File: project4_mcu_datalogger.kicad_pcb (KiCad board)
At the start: 2 copper layers, 29 parts, among them J1 Conn_01x04_Pin, J2 Conn_01x09_Pin, J3 Conn_01x04_Pin, J4 Conn_02x03_Odd_Even, U1 24LC1025, U2 24LC1025, U3 ATMEGA328P-AU, U4 DS1337S_T_R, Y1 32.768 KHz, Y2 16 MHz

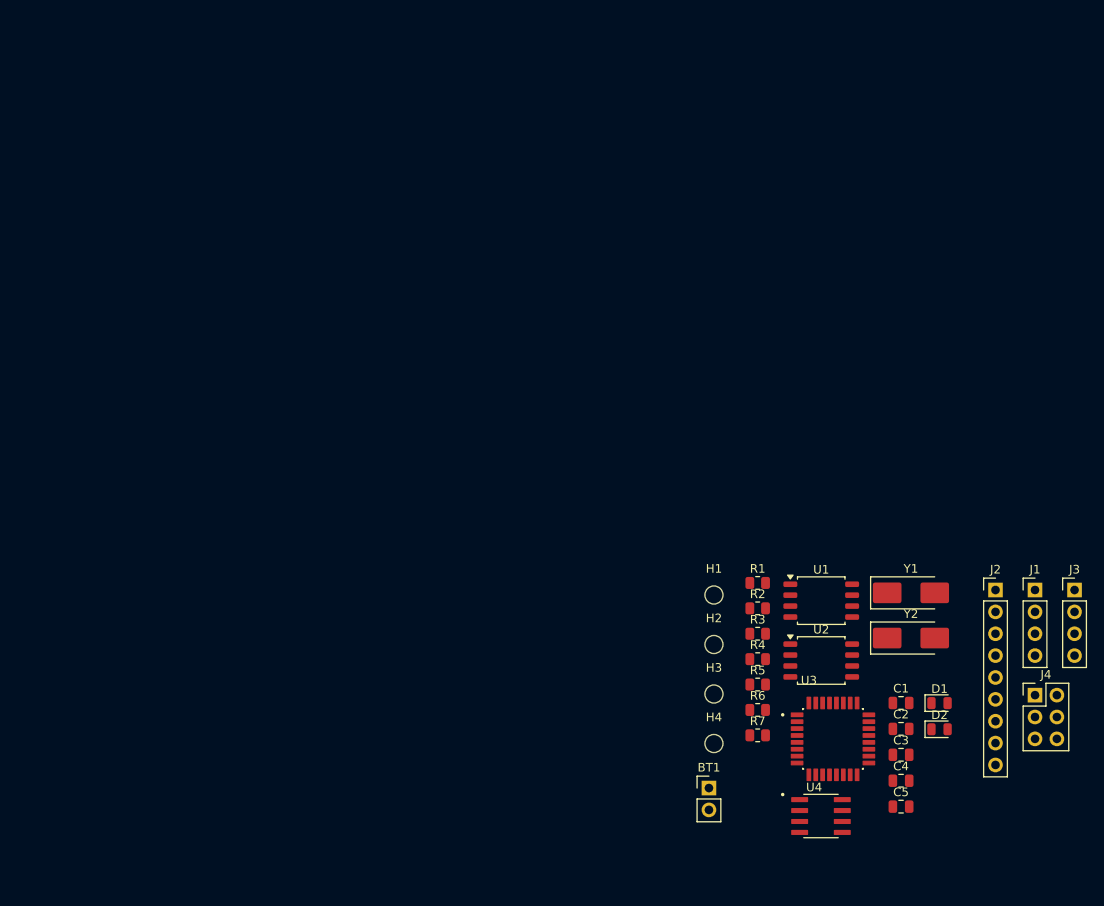
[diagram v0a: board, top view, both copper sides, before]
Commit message: Completed placement of footprints
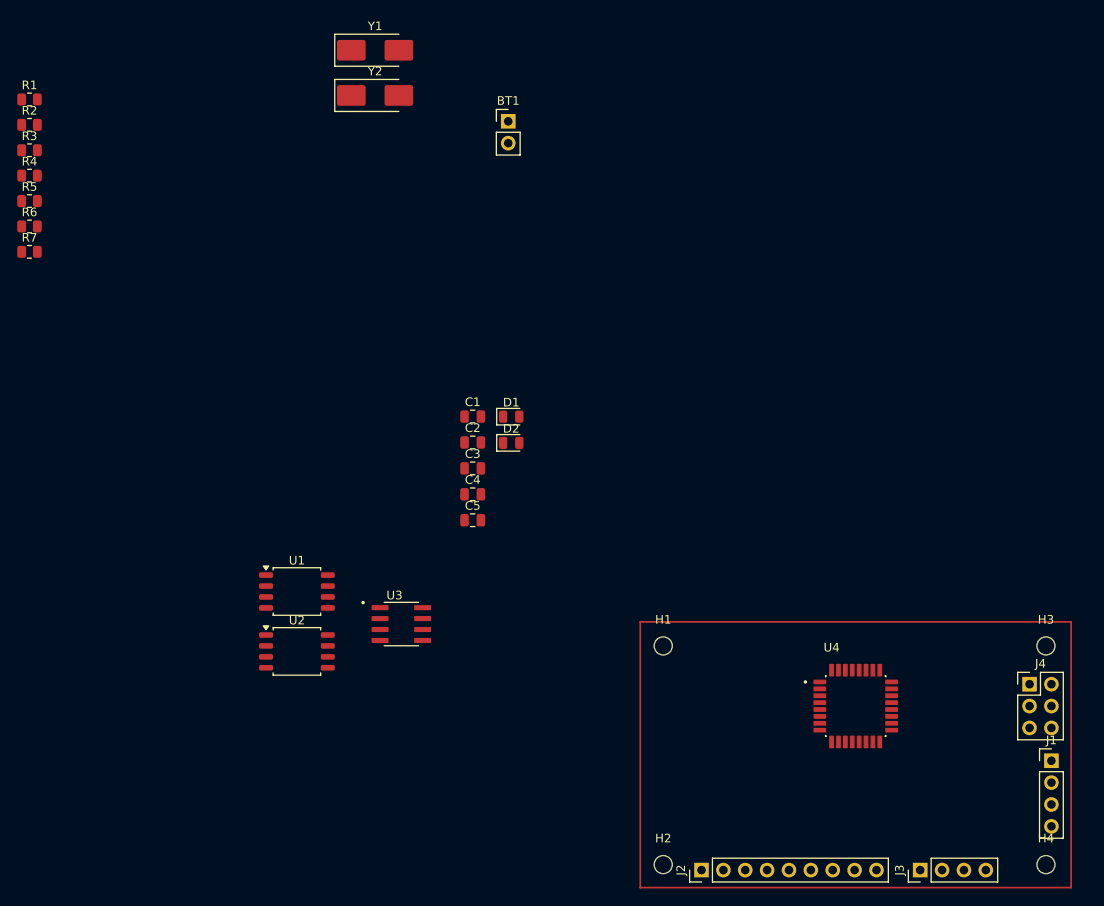
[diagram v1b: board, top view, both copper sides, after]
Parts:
- moved R1 101.5 mm to (54.0, 39.4)
- moved R2 101.5 mm to (54.0, 42.4)
- moved R3 101.5 mm to (54.0, 45.3)
- moved R4 101.5 mm to (54.0, 48.2)
- moved R5 101.5 mm to (54.0, 51.2)
- moved R6 101.5 mm to (54.0, 54.1)
- moved R7 101.5 mm to (54.0, 57.1)
- moved Y1 88.6 mm to (94.2, 33.7)
- moved Y2 88.6 mm to (94.2, 38.9)
- moved BT1 80.9 mm to (109.6, 41.9)
- moved U1 60.9 mm to (85.1, 96.5)
- moved U2 60.9 mm to (85.1, 103.5)
- moved C1 59.8 mm to (105.5, 76.2)
- moved C2 59.8 mm to (105.5, 79.2)
- moved C3 59.8 mm to (105.5, 82.2)
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- renumbered U4 to U3, U3 to U4

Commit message: Completed PCB routing
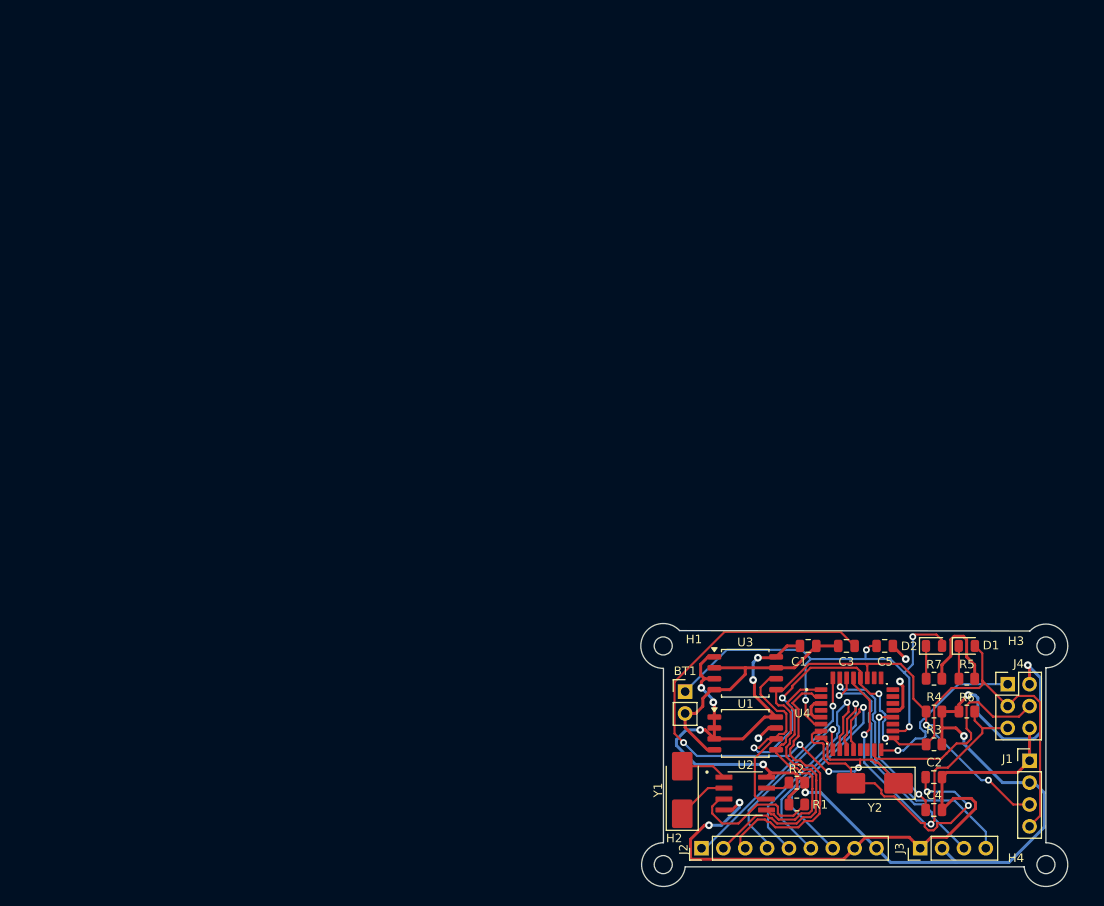
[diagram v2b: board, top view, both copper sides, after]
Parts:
- U2: value 24LC1025 -> DS1337S_T_R; footprint Package_SO:SOIC-8_5.3x5.3mm_P1.27mm -> DS1337S_T_R:SOIC127P600X175-8N
- U3: value DS1337S_T_R -> 24LC1025; footprint DS1337S_T_R:SOIC127P600X175-8N -> Package_SO:SOIC-8_5.3x5.3mm_P1.27mm
- moved R3 125.7 mm to (159.1, 114.3), turned to 180 degrees
- moved R6 122.6 mm to (162.9, 110.5)
- moved R5 122.2 mm to (162.9, 106.7), turned to 180 degrees
- moved R4 122.1 mm to (159.1, 110.5), turned to 180 degrees
- moved R1 121.0 mm to (143.2, 121.3)
- moved R2 117.4 mm to (143.2, 118.7), turned to 180 degrees
- moved R7 116.2 mm to (159.1, 106.7)
- moved Y2 98.7 mm to (152.2, 118.8), turned to 180 degrees
- moved Y1 93.0 mm to (129.8, 119.6), turned to 90 degrees
- moved BT1 69.3 mm to (130.2, 108.2)
- moved C2 66.2 mm to (159.1, 118.1), turned to 180 degrees
- moved C4 64.9 mm to (159.1, 121.9), turned to 180 degrees
- moved D1 59.2 mm to (162.9, 102.9)
- moved U2 54.6 mm to (137.2, 120.0)
- moved U1 54.6 mm to (137.2, 113.0)
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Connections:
- C2 pad 2: Net-(U4-PB7) -> Net-(U4-PB6)
- C3 pad 2: Net-(U4-PB6) -> Net-(U4-PB7)
- R1 pad 2: Net-(U3-~{INTA}) -> Net-(U2-~{INTA})
- R2 pad 2: Net-(U3-SQW/~INT) -> Net-(U2-SQW/~INT)
- U2 pad 1: /Vcc -> Net-(U2-X1)
- U2 pad 2: GND -> Net-(U2-X2)
- U2 pad 3: /Vcc -> Net-(U2-~{INTA})
- U2 pad 7: GND -> Net-(U2-SQW/~INT)
- U3 pad 1: Net-(U3-X1) -> /Vcc
- U3 pad 2: Net-(U3-X2) -> GND
- U3 pad 3: Net-(U3-~{INTA}) -> /Vcc
- U3 pad 7: Net-(U3-SQW/~INT) -> GND
- Y1 pad 1: Net-(U3-X2) -> Net-(U2-X2)
- Y1 pad 2: Net-(U3-X1) -> Net-(U2-X1)
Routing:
- net /Vcc: track 0.00 -> 149.1 mm, vias 0 -> 10
- net GND: track 0.00 -> 130.3 mm, vias 0 -> 5
- net /SCK: track 0.00 -> 98.7 mm, vias 0 -> 4
- net Net-(U4-PB7): track 0.00 -> 67.6 mm, vias 0 -> 4
- net /SDA: track 0.00 -> 67.2 mm, vias 0 -> 2
- net Net-(BT1-+): track 0.00 -> 57.7 mm, vias 0 -> 4
- net /RESET: track 0.00 -> 41.2 mm, vias 0 -> 2
- net Net-(U4-PB6): track 0.00 -> 36.0 mm, vias 0 -> 2
- net /D3: track 0.00 -> 33.5 mm
- net /D4: track 0.00 -> 32.9 mm
- net /TX: track 0.00 -> 31.2 mm, vias 0 -> 1
- net /RX: track 0.00 -> 29.2 mm, vias 0 -> 1
- net /D6: track 0.00 -> 27.9 mm, vias 0 -> 1
- net /D7: track 0.00 -> 27.7 mm, vias 0 -> 1
- net /D8: track 0.00 -> 27.5 mm, vias 0 -> 1
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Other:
- board outline added: 49.6 x 30.5 mm

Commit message: Rework of PCB routing
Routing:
- net GND: track 130.3 -> 176.2 mm, vias 5 -> 9
- net Net-(BT1-+): track 57.7 -> 62.2 mm
- net /SDA: track 67.2 -> 66.6 mm

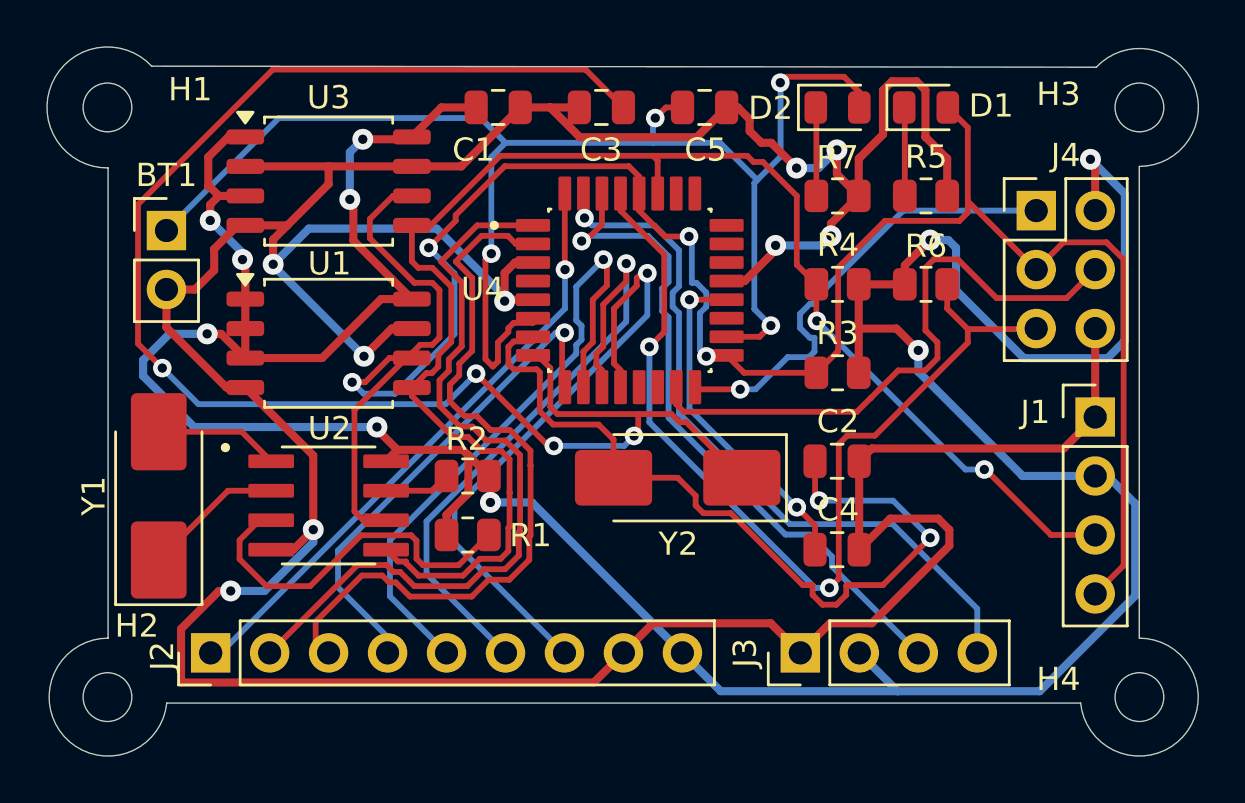
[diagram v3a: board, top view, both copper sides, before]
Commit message: Added copper fills and improved routing
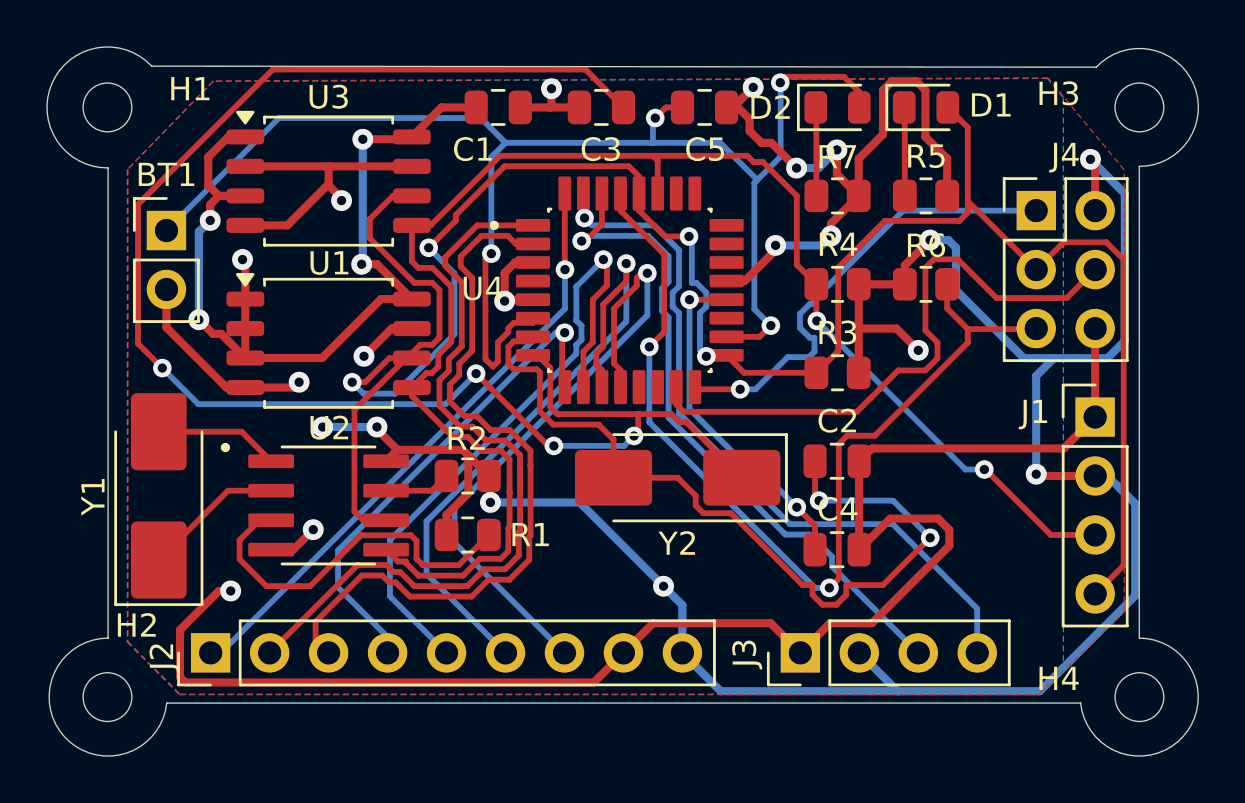
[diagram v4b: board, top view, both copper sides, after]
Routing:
- net GND: track 176.2 -> 131.0 mm, vias 9 -> 12
- net /Vcc: track 149.1 -> 138.3 mm, vias 10 -> 13
- added copper zone on F.Cu, net /Vcc
- added copper zone on B.Cu, net GND

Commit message: Fixed outstanding issues
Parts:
- renumbered J2 to J1, J1 to J2
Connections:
- BT1 pad 1: Net-(BT1-+) -> /Vcc
- C5 pad 1: Net-(BT1-+) -> /Vcc
- D2 pad 2: Net-(BT1-+) -> /Vcc
- U4 pad 18: Net-(BT1-+) -> /Vcc
- U4 pad 6: Net-(BT1-+) -> /Vcc
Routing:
- net Net-(BT1-+): track 62.2 -> 0.00 mm, vias 4 -> 0
- net /Vcc: track 138.3 -> 173.1 mm, vias 13 -> 16
- net GND: track 131.0 -> 138.7 mm, vias 12 -> 11
- net Net-(U2-~{INTA}): track 16.2 -> 20.2 mm
- net Net-(U4-PB7): track 67.6 -> 68.9 mm
- net /SDA: track 66.6 -> 67.9 mm
- net /SCK: track 98.7 -> 99.3 mm
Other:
- board text added: "2"
- board text added: "3"
- board text added: "4"
- board text added: "5"
- board text added: "6"
- board text added: "7"
- board text added: "8"
- board text added: "GND"
- board text added: "GPIO"
- board text added: "I2C"
- board text added: "ICSP"
- board text added: "ICSP MISO | Vcc SCK | MOSI RESET | GND"
- board text added: "RX"
- board text added: "SCK"
- board text added: "SDA"
- board text added: "SERIAL"
- board text added: "TX"
- board text added: "Vcc"

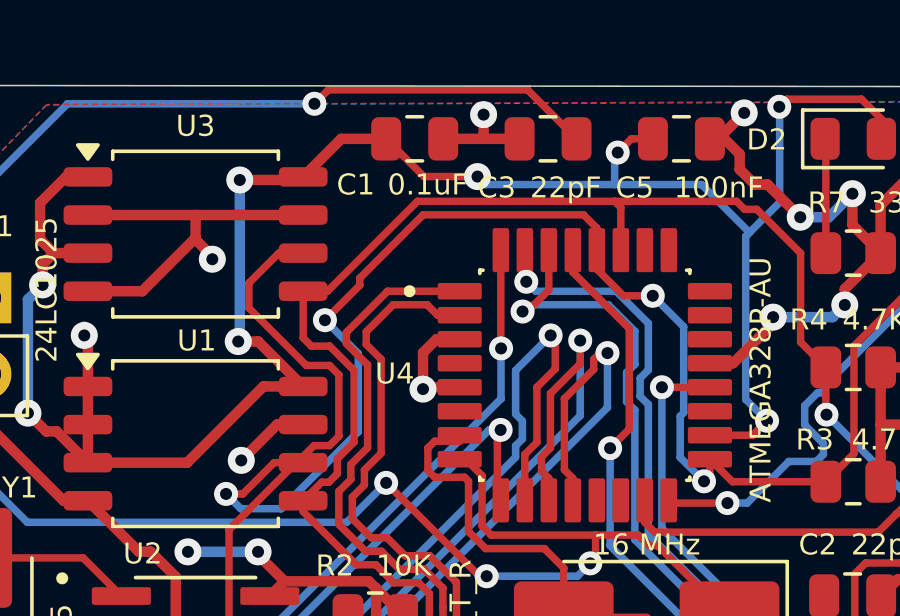
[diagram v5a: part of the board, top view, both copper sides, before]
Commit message: Added back silkscreen
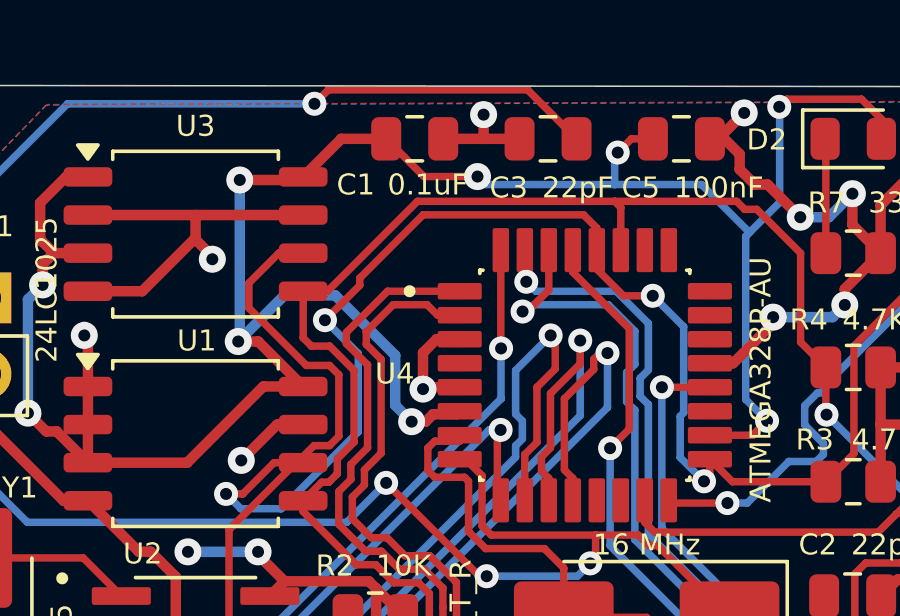
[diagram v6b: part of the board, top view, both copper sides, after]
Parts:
- added REF**: KiCad-Logo2_5mm_SilkScreen, Symbol:KiCad-Logo2_5mm_SilkScreen, B.Cu at (139.1, 106.0)
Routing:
- net /Vcc: track 173.1 -> 184.0 mm, vias 16 -> 17
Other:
- board text added: "- 2Mbit EEPROM - RTC - I2C, SPI, GPIOs"
- board text added: "Datalogger with the ATMega328P."
